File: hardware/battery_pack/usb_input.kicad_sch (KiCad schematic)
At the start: 56 parts, among them J201 USB_C_Receptacle_USB2.0, J202 Conn_01x02_Male, Q201 SQJ951EP, U201 BSS84DW, U202 CYPD3177, U203 T2N7002AK

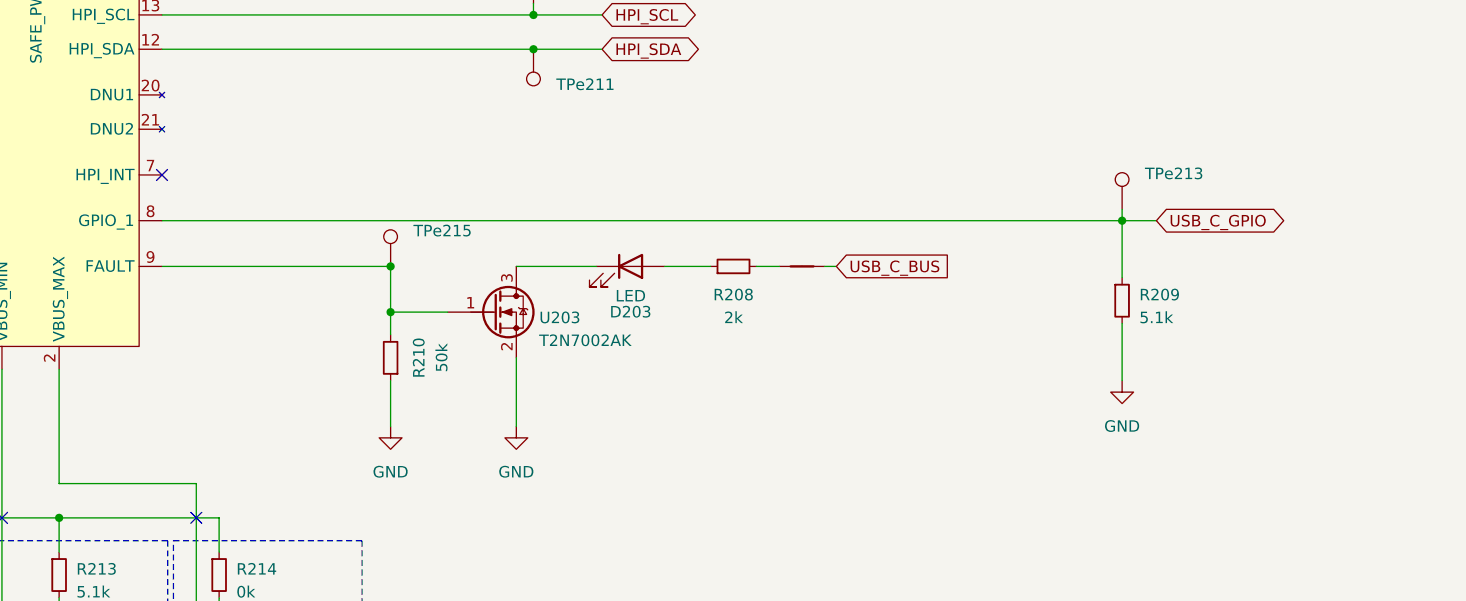
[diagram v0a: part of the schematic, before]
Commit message: Finished routing. Finall review and re-annotation pending.
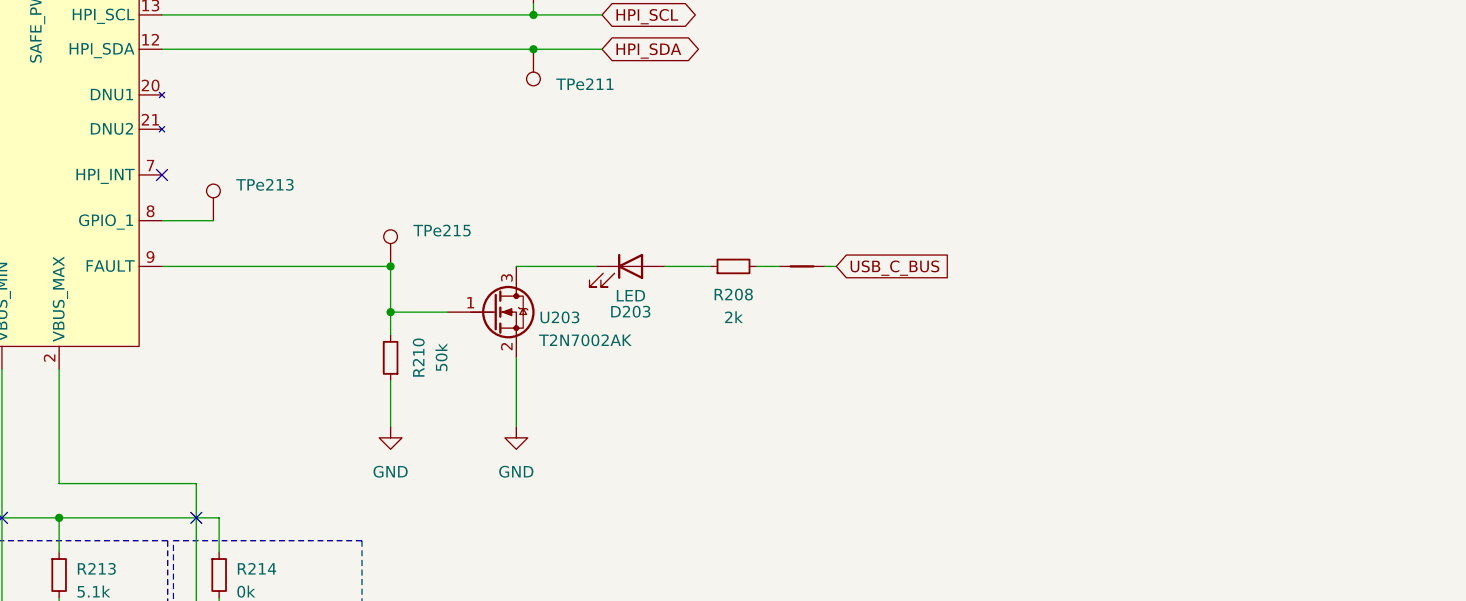
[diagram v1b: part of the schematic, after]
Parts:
- removed R209: 5.1k, Resistor_SMD:R_0805_2012Metric_Pad1.20x1.40mm_HandSolder, symbol Device:R_Small
- U202: footprint Package_DFN_QFN:QFN-24-1EP_4x4mm_P0.5mm_EP2.75x2.75mm -> Package_DFN_QFN:QFN-24-1EP_4x4mm_P0.5mm_EP2.65x2.65mm
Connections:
- net GND: now also U202.25 (TP)
- net USB_C_GPIO: no longer names the net of TPe213.1, U202.8 (GPIO_1)
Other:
- moved on the sheet: TPe213
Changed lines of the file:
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@@
 	)
 	(junction
-		(at 350.52 175.26)
-		(diameter 0)
-		(color 0 0 0 0)
-	)
-	(junction
 		(at 166.37 69.85)
 		(diameter 0)
@@
 	(wire
 		(pts
-			(xy 350.52 175.26) (xy 350.52 173.99)
-		)
-		(stroke
-			(width 0)
-			(type default)
-		)
-	)
-	(wire
-		(pts
 			(xy 226.06 127) (xy 226.06 124.46)
 		)
@@
 	(wire
 		(pts
-			(xy 243.84 175.26) (xy 350.52 175.26)
+			(xy 243.84 175.26) (xy 249.555 175.26)
 		)
 		(stroke
@@
 	(wire
 		(pts
-			(xy 350.52 186.69) (xy 350.52 193.04)
-		)
-		(stroke
-			(width 0)
-			(type default)
-		)
-	)
-	(wire
-		(pts
-			(xy 350.52 175.26) (xy 354.33 175.26)
-		)
-		(stroke
-			(width 0)
-			(type default)
-		)
-	)
-	(wire
-		(pts
 			(xy 80.01 189.23) (xy 83.82 189.23)
 		)
@@
 	(wire
 		(pts
-			(xy 350.52 175.26) (xy 350.52 181.61)
-		)
-		(stroke
-			(width 0)
-			(type default)
-		)
-	)
-	(wire
-		(pts
 			(xy 194.31 102.87) (xy 255.27 102.87)
 		)
@@
 		)
 	)
-	(global_label "USB_C_GPIO"
-		(shape bidirectional)
-		(at 354.33 175.26 0)
-		(fields_autoplaced yes)
-		(effects
-			(font
-				(size 1.27 1.27)
-			)
-			(justify left)
-		)
-		(property "Intersheetrefs" "${INTERSHEET_REFS}"
-			(at 369.8376 175.26 0)
-			(effects
-				(font
-					(size 1.27 1.27)
-				)
-				(justify left)
-				(hide yes)
-			)
-		)
-	)
 	(global_label "V_USB_OUT"
 		(shape output)
@@
 	)
 	(symbol
-		(lib_id "Device:R_Small")
-		(at 350.52 184.15 0)
-		(unit 1)
-		(exclude_from_sim no)
-		(in_bom yes)
-		(on_board yes)
-		(dnp no)
-		(fields_autoplaced yes)
-		(property "Reference" "R209"
-			(at 352.425 183.515 0)
-			(effects
-				(font
-					(size 1.27 1.27)
-				)
-				(justify left)
-			)
-		)
-		(property "Value" "5.1k"
-			(at 352.425 186.055 0)
-			(effects
-				(font
-					(size 1.27 1.27)
-				)
-				(justify left)
-			)
-		)
-		(property "Footprint" "Resistor_SMD:R_0805_2012Metric_Pad1.20x1.40mm_HandSolder"
-			(at 350.52 184.15 0)
-			(effects
-				(font
-					(size 1.27 1.27)
-				)
-				(hide yes)
-			)
-		)
-		(property "Datasheet" "~"
-			(at 350.52 184.15 0)
-			(effects
-				(font
-					(size 1.27 1.27)
-				)
-				(hide yes)
-			)
-		)
-		(property "Description" ""
-			(at 350.52 184.15 0)
-			(effects
-				(font
-					(size 1.27 1.27)
-				)
-				(hide yes)
-			)
-		)
-		(pin "1"
-		)
-		(pin "2"
-		)
-		(instances
-			(project "power_supply"
-				(path "/3169906c-dcce-4761-b072-54530f8b9e50/a50540a9-48b1-49df-82d6-05c97d35c6f8"
-					(reference "R209")
-					(unit 1)
-				)
-			)
-			(project "battery_charging_devboard"
-				(path "/451b7129-01d5-46cf-a4e9-c4e0c27ff0b6/beffddf7-e895-42d7-ba8a-5d365171da10"
-					(reference "R110")
-					(unit 1)
-				)
-			)
-		)
-	)
-	(symbol
 		(lib_id "Device:C_Small")
 		(at 151.13 155.575 0)
@@
 	(symbol
 		(lib_id "Connector:TestPoint")
-		(at 350.52 173.99 0)
+		(at 249.555 175.26 0)
 		(unit 1)
 		(exclude_from_sim no)
@@
 		(fields_autoplaced yes)
 		(property "Reference" "TPe213"
-			(at 353.06 170.053 0)
+			(at 252.095 171.323 0)
 			(effects
 				(font
@@
 		)
 		(property "Value" "TestPoint"
-			(at 353.06 172.593 0)
+			(at 252.095 173.863 0)
 			(effects
 				(font
@@
 		)
 		(property "Footprint" "TestPoint:TestPoint_Pad_D1.0mm"
-			(at 355.6 173.99 0)
+			(at 254.635 175.26 0)
 			(effects
 				(font
@@
 		)
 		(property "Datasheet" "~"
-			(at 355.6 173.99 0)
+			(at 254.635 175.26 0)
 			(effects
 				(font
@@
 		)
 		(property "Description" ""
-			(at 350.52 173.99 0)
+			(at 249.555 175.26 0)
 			(effects
 				(font
@@
 	)
 	(symbol
-		(lib_id "power:GND")
-		(at 350.52 193.04 0)
-		(mirror y)
-		(unit 1)
-		(exclude_from_sim no)
-		(in_bom yes)
-		(on_board yes)
-		(dnp no)
-		(fields_autoplaced yes)
-		(property "Reference" "#PWR0206"
-			(at 350.52 199.39 0)
-			(effects
-				(font
-					(size 1.27 1.27)
-				)
-				(hide yes)
-			)
-		)
-		(property "Value" "GND"
-			(at 350.52 198.12 0)
-			(effects
-				(font
-					(size 1.27 1.27)
-				)
-			)
-		)
-		(property "Footprint" ""
-			(at 350.52 193.04 0)
-			(effects
-				(font
-					(size 1.27 1.27)
-				)
-				(hide yes)
-			)
-		)
-		(property "Datasheet" ""
-			(at 350.52 193.04 0)
-			(effects
-				(font
-					(size 1.27 1.27)
-				)
-				(hide yes)
-			)
-		)
-		(property "Description" ""
-			(at 350.52 193.04 0)
-			(effects
-				(font
-					(size 1.27 1.27)
-				)
-				(hide yes)
-			)
-		)
-		(pin "1"
-		)
-		(instances
-			(project "power_supply"
-				(path "/3169906c-dcce-4761-b072-54530f8b9e50/a50540a9-48b1-49df-82d6-05c97d35c6f8"
-					(reference "#PWR0206")
-					(unit 1)
-				)
-			)
-			(project "battery_charging_devboard"
-				(path "/451b7129-01d5-46cf-a4e9-c4e0c27ff0b6/beffddf7-e895-42d7-ba8a-5d365171da10"
-					(reference "#PWR0105")
-					(unit 1)
-				)
-			)
-		)
-	)
-	(symbol
 		(lib_id "Connector:TestPoint")
 		(at 246.38 147.32 0)
@@
 			)
 		)
-		(property "Footprint" "Package_DFN_QFN:QFN-24-1EP_4x4mm_P0.5mm_EP2.75x2.75mm"
+		(property "Footprint" "Package_DFN_QFN:QFN-24-1EP_4x4mm_P0.5mm_EP2.65x2.65mm"
 			(at 222.25 134.62 0)
 			(effects
@@
 		(pin "16"
 		)
+		(pin "25"
+		)
 		(instances
